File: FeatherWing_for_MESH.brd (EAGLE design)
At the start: 50.8 x 22.9 mm, 21 parts, among them J1 NF, J2 NF

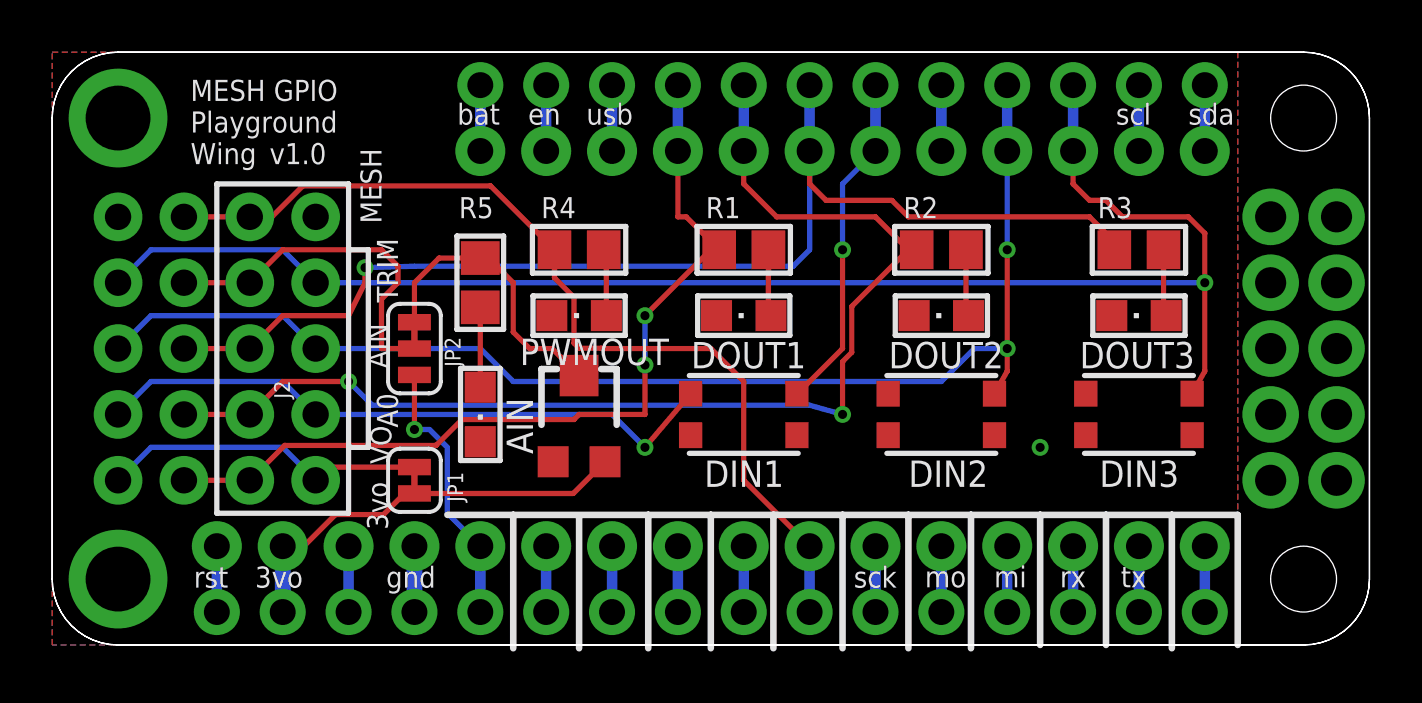
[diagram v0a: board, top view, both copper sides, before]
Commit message: v1.1 Add Mesh pin1 marking, move LEDs away from buttons, default not to connect 3V and Vout. Panelized garber.
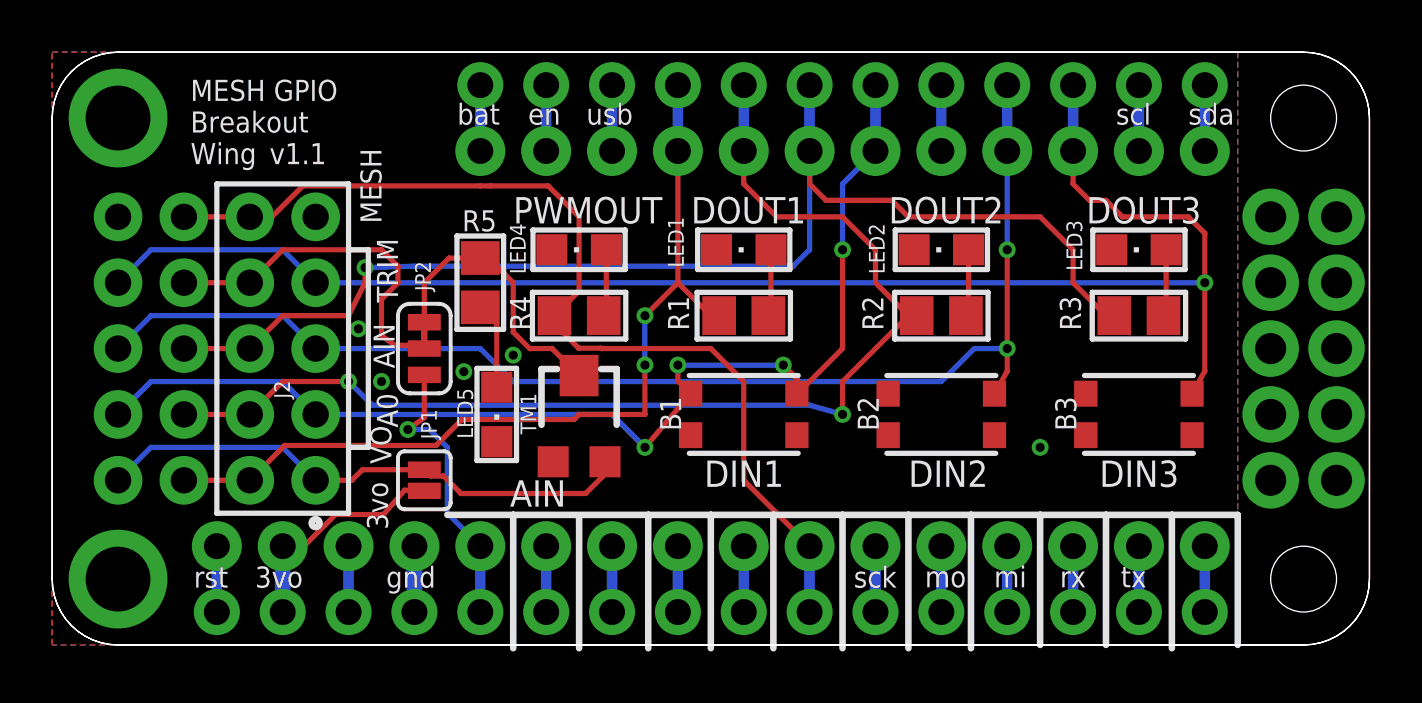
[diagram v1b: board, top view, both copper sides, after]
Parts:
- JP1: value JUMPER-SMT_2_NC_TRACE_SILK -> JUMPER-SMT_2_NO_SILK; device SparkFun-Jumpers:SMT-JUMPER_2_NC_TRACE_SILK -> SparkFun-Jumpers:SMT-JUMPER_2_NO_SILK
- moved LED1 2.54 mm to (26.7, 15.2)
- moved LED2 2.54 mm to (34.3, 15.2)
- moved LED3 2.54 mm to (41.9, 15.2)
- moved LED4 2.54 mm to (20.3, 15.2)
- moved R1 2.54 mm to (26.7, 12.7)
- moved R2 2.54 mm to (34.3, 12.7)
- moved R3 2.54 mm to (41.9, 12.7)
- moved R4 2.54 mm to (20.3, 12.7)
- moved LED5 0.63 mm to (17.1, 8.89)
- moved JP1 0.38 mm to (14.4, 6.35)
- moved JP2 0.38 mm to (14.4, 11.4)
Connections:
- net 3V: no longer TM1.3
- net VO: now also TM1.3
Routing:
- net VO: track 12.7 -> 21.2 mm
- net 3V: track 16.3 -> 8.94 mm
- net DIN1: track 37.8 -> 44.5 mm, vias 2 -> 4
- net PWMOUT: track 36.8 -> 38.9 mm
- net DOUT3: track 46.9 -> 48.5 mm
- net DOUT2: track 45.3 -> 44.5 mm
- net A0: track 10.5 -> 11.1 mm
- net DOUT1: track 33.7 -> 34.2 mm
- net GND: vias 1 -> 5
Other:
- board text added: "MESH GPIO Breakout Wing"
- board text added: "v1.1"
- board text removed: "MESH GPIO Playground Wing"
- board text removed: "v1.0"
